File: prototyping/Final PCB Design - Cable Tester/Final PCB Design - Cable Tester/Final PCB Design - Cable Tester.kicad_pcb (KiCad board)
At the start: 2 copper layers, 86 x 54 mm, 41 parts, among them J17 Banana Jack, J20 SFML-110-02-L-D-A, J3 Debug Connection, J4 MEM2061-01-188-00-A_REVA, J5 Barrel Jack 9V, J6 Touchscreen HMI, Q1 2N3904, SW1 Rocker Switch, U1 AVR128DB64x-xMR, U2 LP2985-3.3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

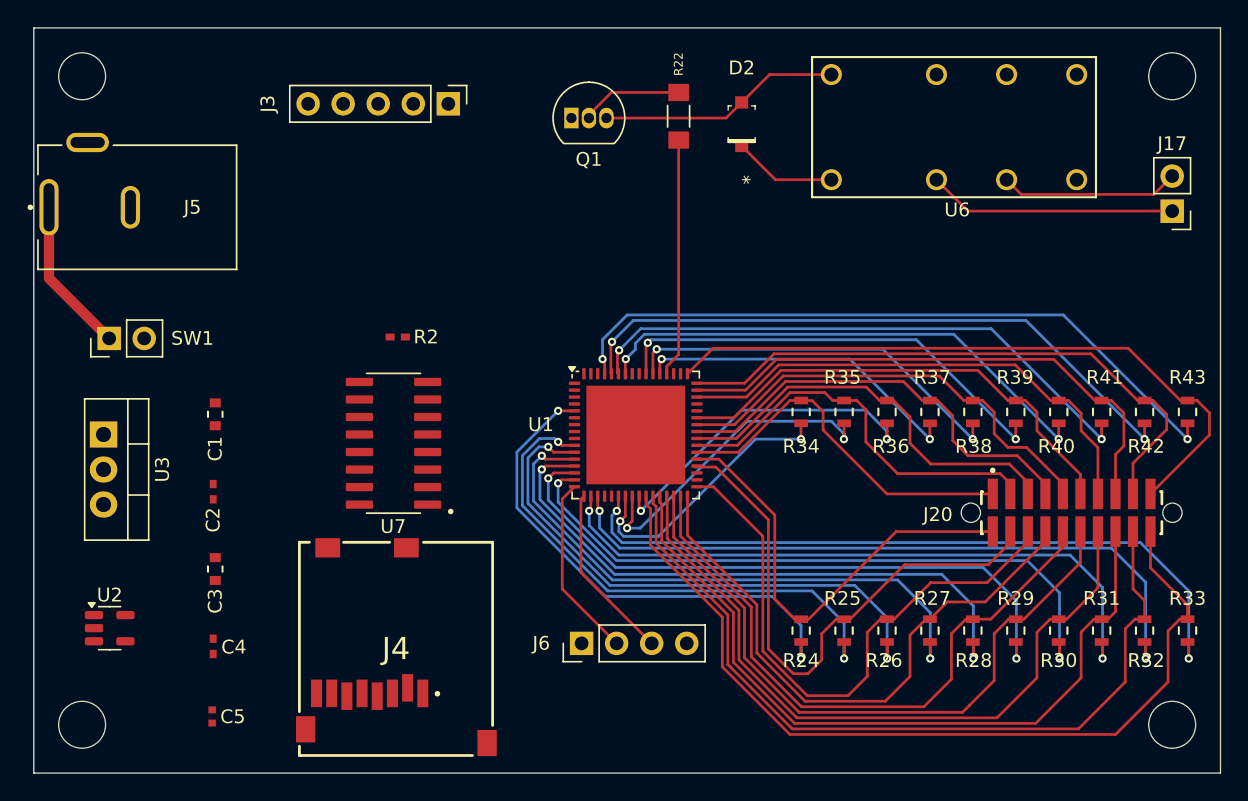
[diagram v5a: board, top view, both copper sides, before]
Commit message: Update - Final PCB design
Added more traces, added and fixed 3D footprints, other minor fixes
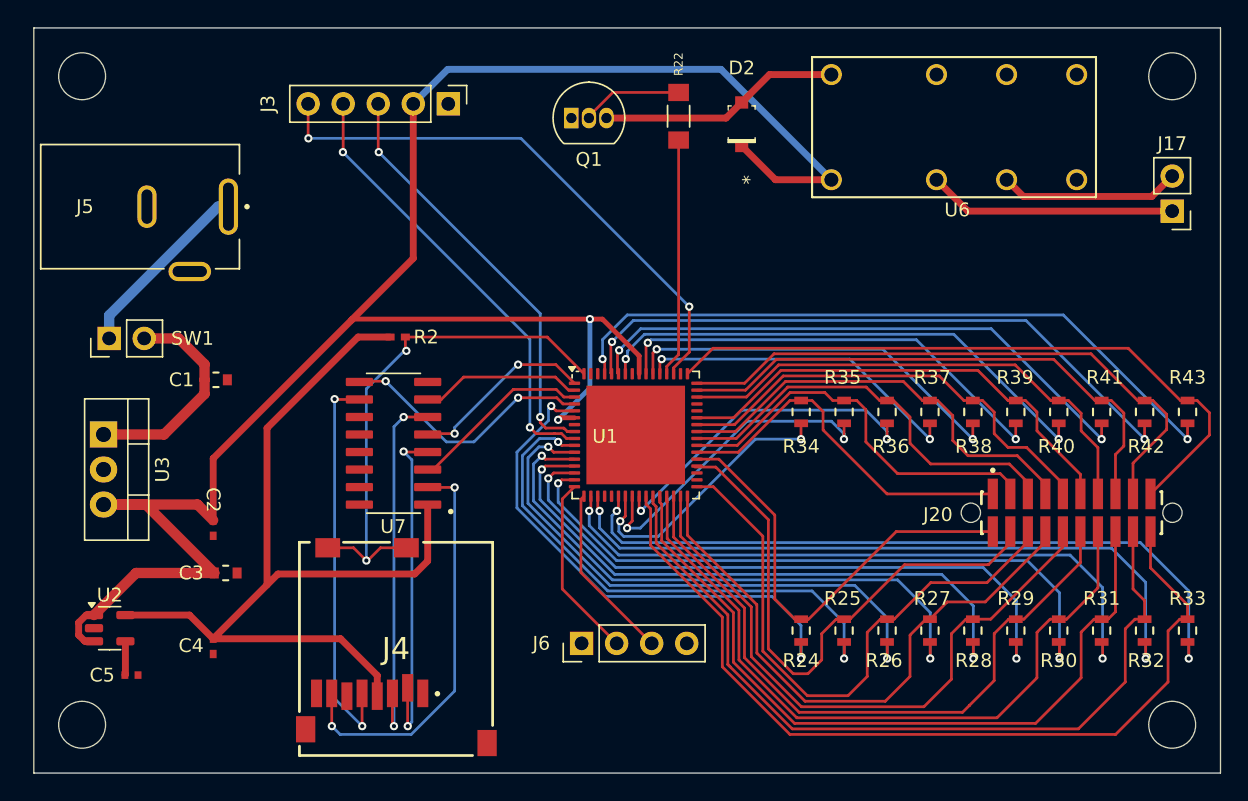
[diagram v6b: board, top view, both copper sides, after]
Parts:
- moved C5 6.57 mm to (98.6, 112.9), turned to 0 degrees
- moved C2 2.65 mm to (104.5, 102.3), turned to -90 degrees
- moved C1 2.50 mm to (104.7, 91.5), turned to 0 degrees
- moved J5 1.20 mm to (99.7, 79.0), turned to -90 degrees
- moved C3 0.81 mm to (105.4, 105.5), turned to 0 degrees
- turned C4 to -90 degrees
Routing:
- net +5V: track 7.51 -> 143.1 mm, vias 0 -> 2
- net +3.3V: track 0.00 -> 66.6 mm
- net UPDI: track 0.00 -> 40.5 mm, vias 0 -> 2
- net CD: track 0.00 -> 38.0 mm, vias 0 -> 2
- net RxD: track 0.00 -> 32.6 mm, vias 0 -> 2
- net TxD: track 0.00 -> 30.7 mm, vias 0 -> 2
- net /mSD_DO: track 0.00 -> 29.5 mm, vias 0 -> 2
- net /mSD_CLK: track 0.00 -> 28.7 mm, vias 0 -> 2
- net /mSD_DI: track 0.00 -> 26.9 mm, vias 0 -> 2
- net /mSD_CS: track 0.00 -> 24.8 mm, vias 0 -> 2
- net CLK: track 0.00 -> 18.9 mm, vias 0 -> 2
- net Net-(SW1A-B): track 0.00 -> 15.8 mm
- net CS: track 0.00 -> 13.6 mm, vias 0 -> 2
- net DO: track 0.00 -> 13.3 mm
- net DI: track 0.00 -> 11.7 mm
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
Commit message: Updated - Final PCB
Added GND fill, places the rest of the trace lines, minor line adjustments.
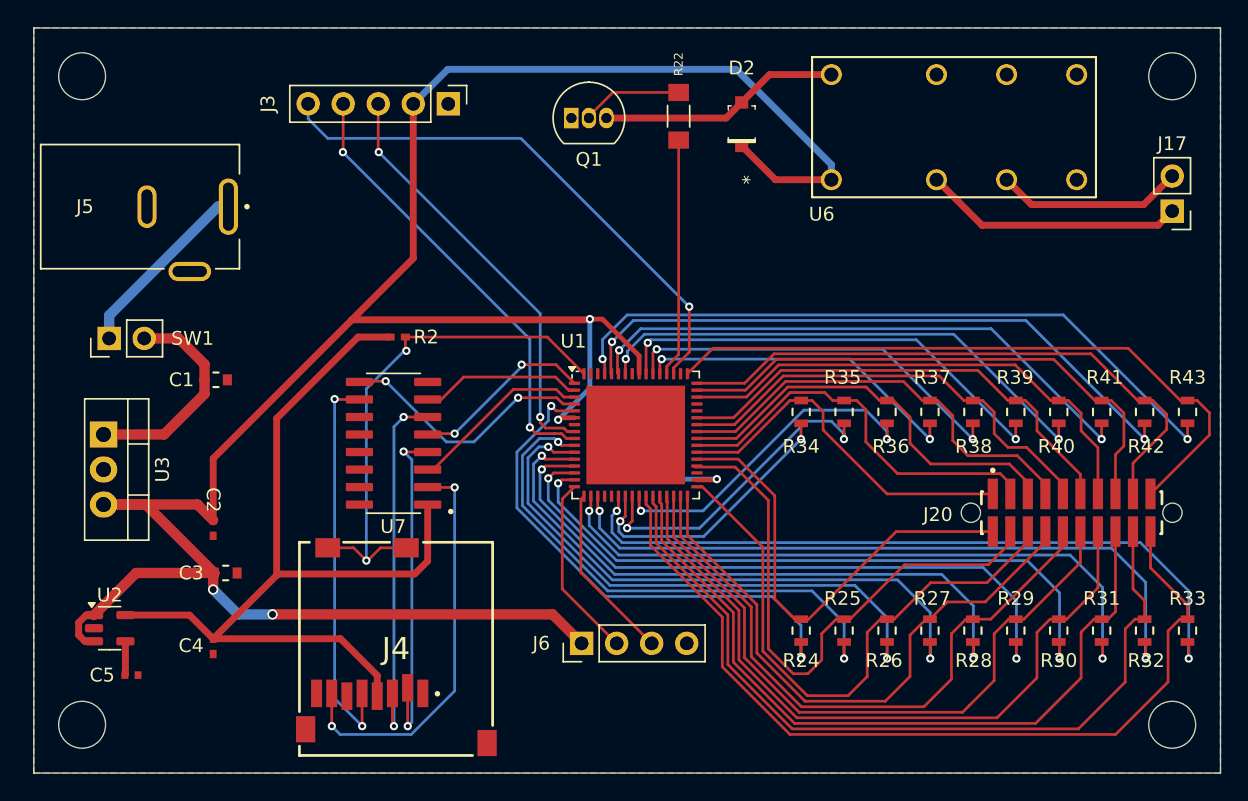
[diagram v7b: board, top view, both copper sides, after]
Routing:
- net +5V: track 143.1 -> 186.7 mm, vias 2 -> 5
- net +3.3V: track 66.6 -> 65.6 mm
- net Net-(J17-Pin_1): track 18.0 -> 18.9 mm
- net ADC 2: track 40.4 -> 41.2 mm
- net ADC 1: track 32.4 -> 33.3 mm
- net UPDI: track 40.5 -> 39.7 mm, vias 2 -> 1
- added copper zone on B.Cu, net GND
- added copper zone on F.Cu, net GND

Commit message: Updated Final PCB
Minor fixes and changes. Moved some traces to not overlap from top and bottom traces
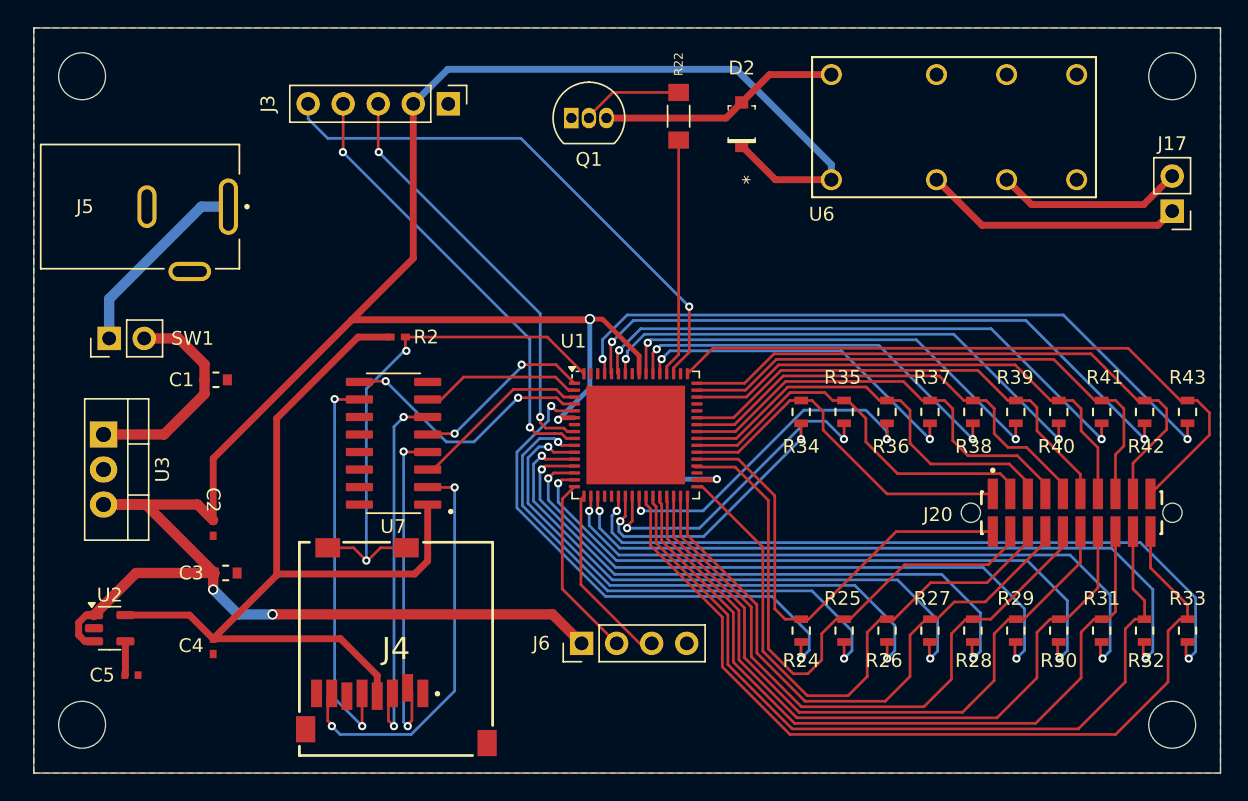
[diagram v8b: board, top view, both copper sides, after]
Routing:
- net /9V: track 13.6 -> 14.3 mm
- net CTRL 6: track 46.0 -> 46.5 mm
- net CTRL 7: track 47.7 -> 48.2 mm
- net CTRL 8: track 47.6 -> 48.1 mm
- net Rx1: track 12.9 -> 13.4 mm
- net CTRL 9: track 50.3 -> 50.8 mm
- net CTRL 10: track 52.5 -> 53.0 mm
